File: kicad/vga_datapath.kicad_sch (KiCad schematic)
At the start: 28 parts, among them Q3 BC547, Q4 BC547, Q5 BC547, U21 74HC377, U23 2764, U24 74HC166, U27 HM62256BLP, U30 74HC377, U32 74HC157

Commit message: hw: finish routing
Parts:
- U23: value 2764 -> 27C64
- U27: value HM62256BLP -> 62256
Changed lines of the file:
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@@
 			)
 		)
-		(property "Value" "2764"
+		(property "Value" "27C64"
 			(at 172.3741 34.29 0)
 			(effects
@@
 			)
 		)
-		(property "Value" "HM62256BLP"
+		(property "Value" "62256"
 			(at 91.0433 43.18 0)
 			(effects

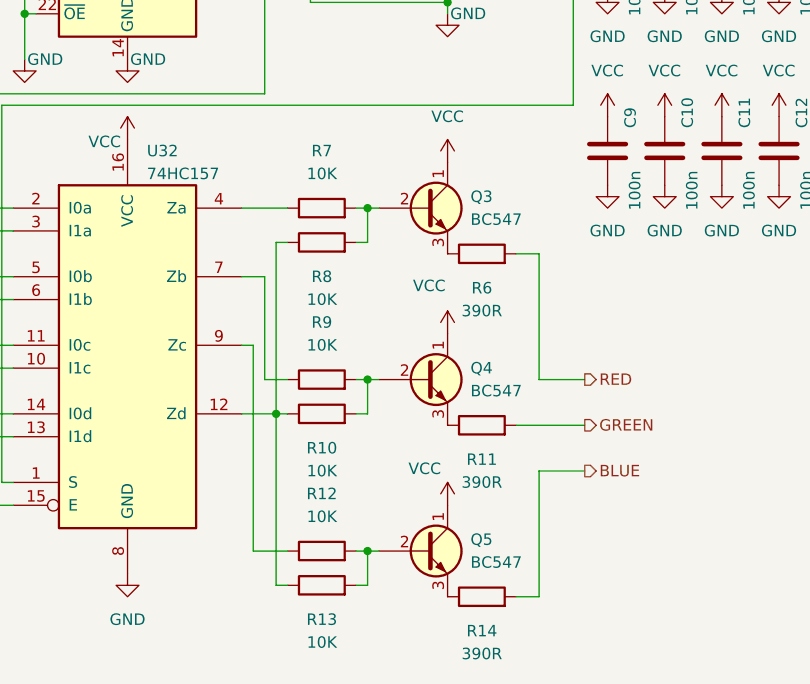
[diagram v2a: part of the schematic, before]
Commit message: hw/vga: reduce resistance in DAC to impove image sharpness
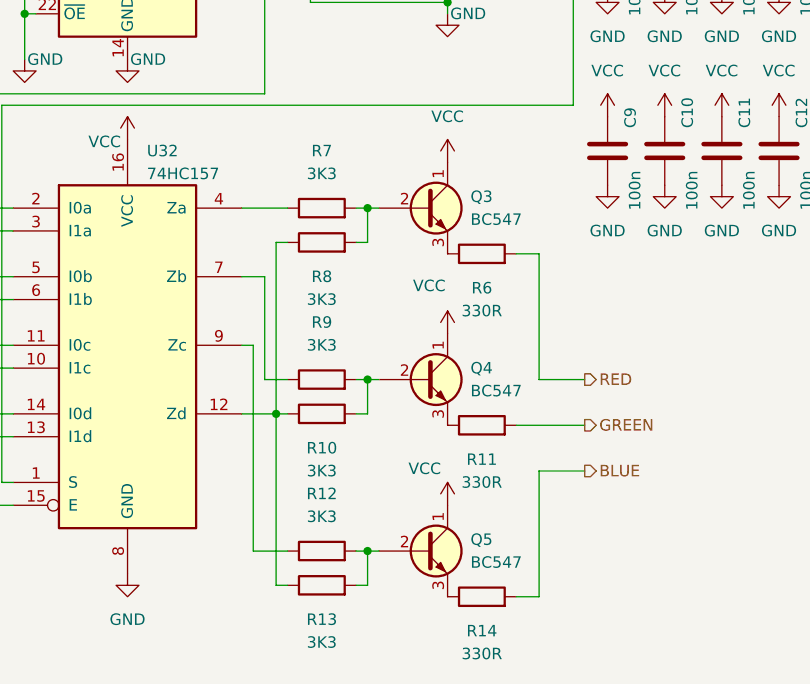
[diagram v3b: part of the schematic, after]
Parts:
- R10, R12, R13, R7, R8, R9: value 10K -> 3K3
- R11, R14, R6: value 390R -> 330R
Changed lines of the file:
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@@
 			)
 		)
-		(property "Value" "10K"
+		(property "Value" "3K3"
 			(at 191.77 133.35 90)
 			(effects
@@
 			)
 		)
-		(property "Value" "390R"
+		(property "Value" "330R"
 			(at 209.55 115.57 90)
 			(effects
@@
 			)
 		)
-		(property "Value" "10K"
+		(property "Value" "3K3"
 			(at 191.77 152.4 90)
 			(effects
@@
 			)
 		)
-		(property "Value" "10K"
+		(property "Value" "3K3"
 			(at 191.77 138.43 90)
 			(effects
@@
 			)
 		)
-		(property "Value" "10K"
+		(property "Value" "3K3"
 			(at 191.77 119.38 90)
 			(effects
@@
 			)
 		)
-		(property "Value" "10K"
+		(property "Value" "3K3"
 			(at 191.77 114.3 90)
 			(effects
@@
 			)
 		)
-		(property "Value" "390R"
+		(property "Value" "330R"
 			(at 209.55 134.62 90)
 			(effects
@@
 			)
 		)
-		(property "Value" "390R"
+		(property "Value" "330R"
 			(at 209.55 153.67 90)
 			(effects
@@
 			)
 		)
-		(property "Value" "10K"
+		(property "Value" "3K3"
 			(at 191.77 100.33 90)
 			(effects
